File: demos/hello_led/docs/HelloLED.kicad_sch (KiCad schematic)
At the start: 2 parts

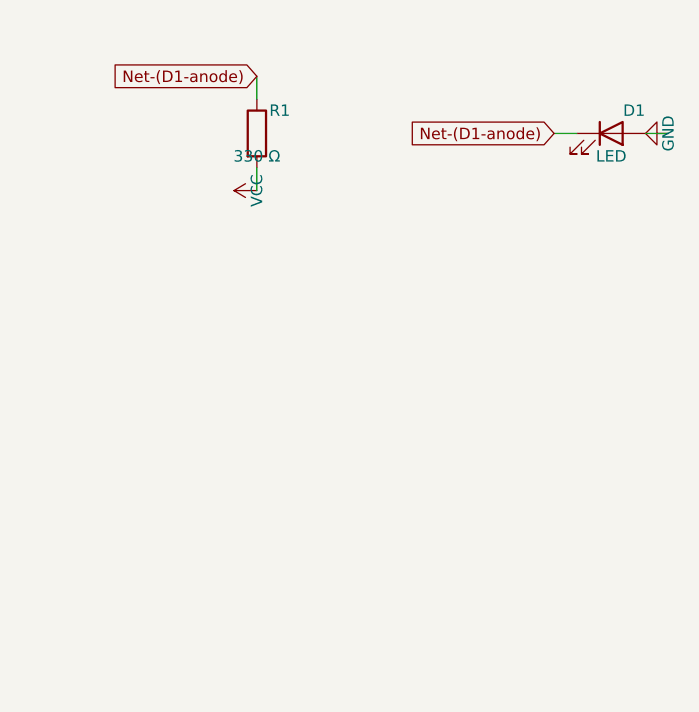
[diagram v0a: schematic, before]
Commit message: export: kicad_sch — Phase 2.5b: layered placement, wire routing, KiCad 10 compatibility (#23)
* export: kicad_sch — Phase 2.5b: layered placement + routing + KiCad 9 fix

Placement (placement.py, complete rewrite):
- Replaces naive grid with Layered Signal Flow algorithm (spec §5 stages 1–8)
- Stage 1: band classification — power chips/rails at top, LEDs at bottom,
  everything else in the signal band
- Stage 2: signal-flow DAG via BFS from Rail/Connector sources; layer = BFS
  distance from nearest source
- Stage 3–4: place within (band, layer) cells at 1500-mil (38.1 mm) same-band
  spacing, 1000-mil inter-band gutter, 25.4 mm page margin
- Stage 6: cluster breakup — up to 10 iterations shifting same-band parts
  that land closer than 0.9× SAME_BAND_SPACING_MM
- Stage 8: page sized to fit (A4 → A3 → A2 → A1)
- grid_place() and sheet_size_mm() kept as shims for backward-compat

Routing (routing.py, new file):
- route_net(): connects stub ends with Manhattan L-shapes (horizontal first)
- find_junctions(): returns points where ≥3 wire endpoints coincide
- renderer uses routed wires between signal-net stub ends

Hierarchical (hierarchical.py, new file):
- collect_boards(), is_multi_board(), sub_sheet_filename() — interface stub
  for multi-Board sub-sheet emission (full implementation deferred)

KiCad 9 sub-symbol name fix (library_loader.py):
- KiCad 9 schematics expect sub-symbols nested inside their parent in
  lib_symbols to use the bare name (R_0_1, LED_0_1, 4069_1_0) — NOT the
  lib-qualified name (Device:R_0_1, Device:LED_0_1, 4xxx:4069_1_0)
- Fixed _qualify_names() to add the lib: prefix only to the exact parent
  symbol name using a lookahead (?=") that prevents sub-unit names from
  being qualified

Tests (+25 tests):
- test_placement.py: band classification, all-on-grid, determinism,
  minimum spacing, power < signal < indicator Y ordering, page sizing
- test_routing.py: H/V segments, L-shapes, orthogonality, grid snap,
  junction detection

Golden files re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
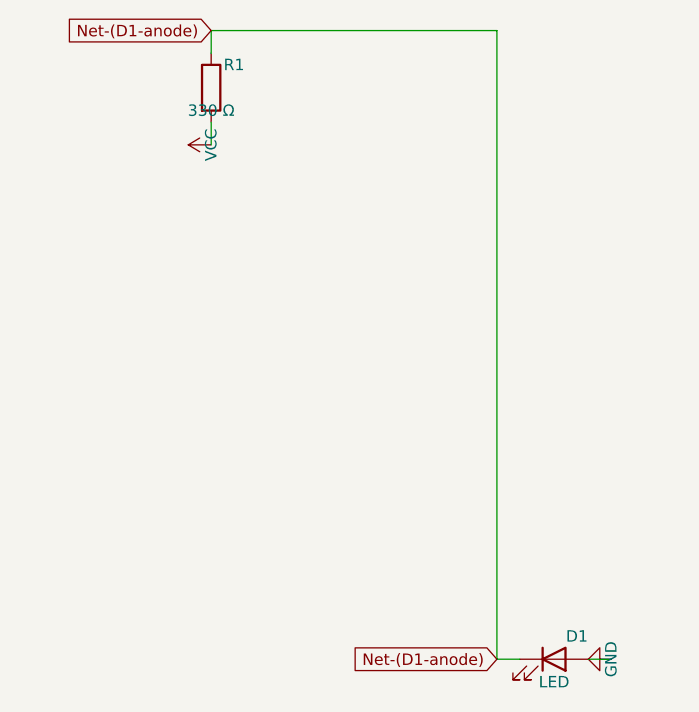
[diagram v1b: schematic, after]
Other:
- moved on the sheet: D1, R1
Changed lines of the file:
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@@
 (kicad_sch
-  (version 20240618)
+  (version 20250114)
   (generator "wirebench")
-  (generator_version "0.1")
+  (generator_version "0.2")
   (paper "A4")
   (symbol
     (lib_id "Device:R")
-    (at 30.48 30.48 0)
+    (at 25.4 25.4 0)
     (unit 1)
     (exclude_from_sim no)
@@
     (dnp no)
     (property "Reference" "R1"
-      (at 33.02 27.94 0)
+      (at 27.94 22.86 0)
       (effects (font (size 1.27 1.27)))
     )
     (property "Value" "330 Ω"
-      (at 30.48 33.02 0)
+      (at 25.4 27.94 0)
       (effects (font (size 1.27 1.27)))
     )
@@
   )
   (wire
-    (pts (xy 30.48 34.29) (xy 30.48 36.83))
+    (pts (xy 25.4 29.21) (xy 25.4 31.75))
     (stroke (width 0) (type default))
   )
   (symbol
     (lib_id "power:VCC")
-    (at 30.48 36.83 90)
+    (at 25.4 31.75 90)
     (unit 1)
     (exclude_from_sim no)
@@
     (dnp no)
     (property "Reference" "#PWR"
-      (at 30.48 36.83 0)
+      (at 25.4 31.75 0)
       (effects (font (size 1.27 1.27)) (hide yes))
     )
     (property "Value" "VCC"
-      (at 30.48 36.83 0)
+      (at 25.4 31.75 0)
       (effects (font (size 1.27 1.27)))
     )
@@
   )
   (wire
-    (pts (xy 30.48 26.67) (xy 30.48 24.13))
+    (pts (xy 25.4 21.59) (xy 25.4 19.05))
     (stroke (width 0) (type default))
   )
   (global_label "Net-(D1-anode)"
     (shape input)
-    (at 30.48 24.13 0)
+    (at 25.4 19.05 0)
     (fields_autoplaced yes)
     (effects (font (size 1.27 1.27)) (justify right))
@@
   (symbol
     (lib_id "Device:LED")
-    (at 69.85 30.48 0)
+    (at 63.5 88.9 0)
     (unit 1)
     (exclude_from_sim no)
@@
     (dnp no)
     (property "Reference" "D1"
-      (at 72.39 27.94 0)
+      (at 66.04 86.36 0)
       (effects (font (size 1.27 1.27)))
     )
     (property "Value" "LED"
-      (at 69.85 33.02 0)
+      (at 63.5 91.44 0)
       (effects (font (size 1.27 1.27)))
     )
@@
   )
   (wire
-    (pts (xy 66.04 30.48) (xy 63.5 30.48))
+    (pts (xy 59.69 88.9) (xy 57.15 88.9))
     (stroke (width 0) (type default))
   )
   (global_label "Net-(D1-anode)"
     (shape input)
-    (at 63.5 30.48 0)
+    (at 57.15 88.9 0)
     (fields_autoplaced yes)
     (effects (font (size 1.27 1.27)) (justify right))
@@
   )
   (wire
-    (pts (xy 73.66 30.48) (xy 76.2 30.48))
+    (pts (xy 67.31 88.9) (xy 69.85 88.9))
     (stroke (width 0) (type default))
   )
   (symbol
     (lib_id "power:GND")
-    (at 76.2 30.48 270)
+    (at 69.85 88.9 270)
     (unit 1)
     (exclude_from_sim no)
@@
     (dnp no)
     (property "Reference" "#PWR"
-      (at 76.2 30.48 0)
+      (at 69.85 88.9 0)
       (effects (font (size 1.27 1.27)) (hide yes))
     )
     (property "Value" "GND"
-      (at 76.2 30.48 0)
+      (at 69.85 88.9 0)
       (effects (font (size 1.27 1.27)))
     )
     (pin "1")
   )
+  (wire
+    (pts (xy 25.4 19.05) (xy 57.15 19.05))
+    (stroke (width 0) (type default))
+  )
+  (wire
+    (pts (xy 57.15 19.05) (xy 57.15 88.9))
+    (stroke (width 0) (type default))
+  )
   (sheet_instances
